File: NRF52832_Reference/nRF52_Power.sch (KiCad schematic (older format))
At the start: 21 parts

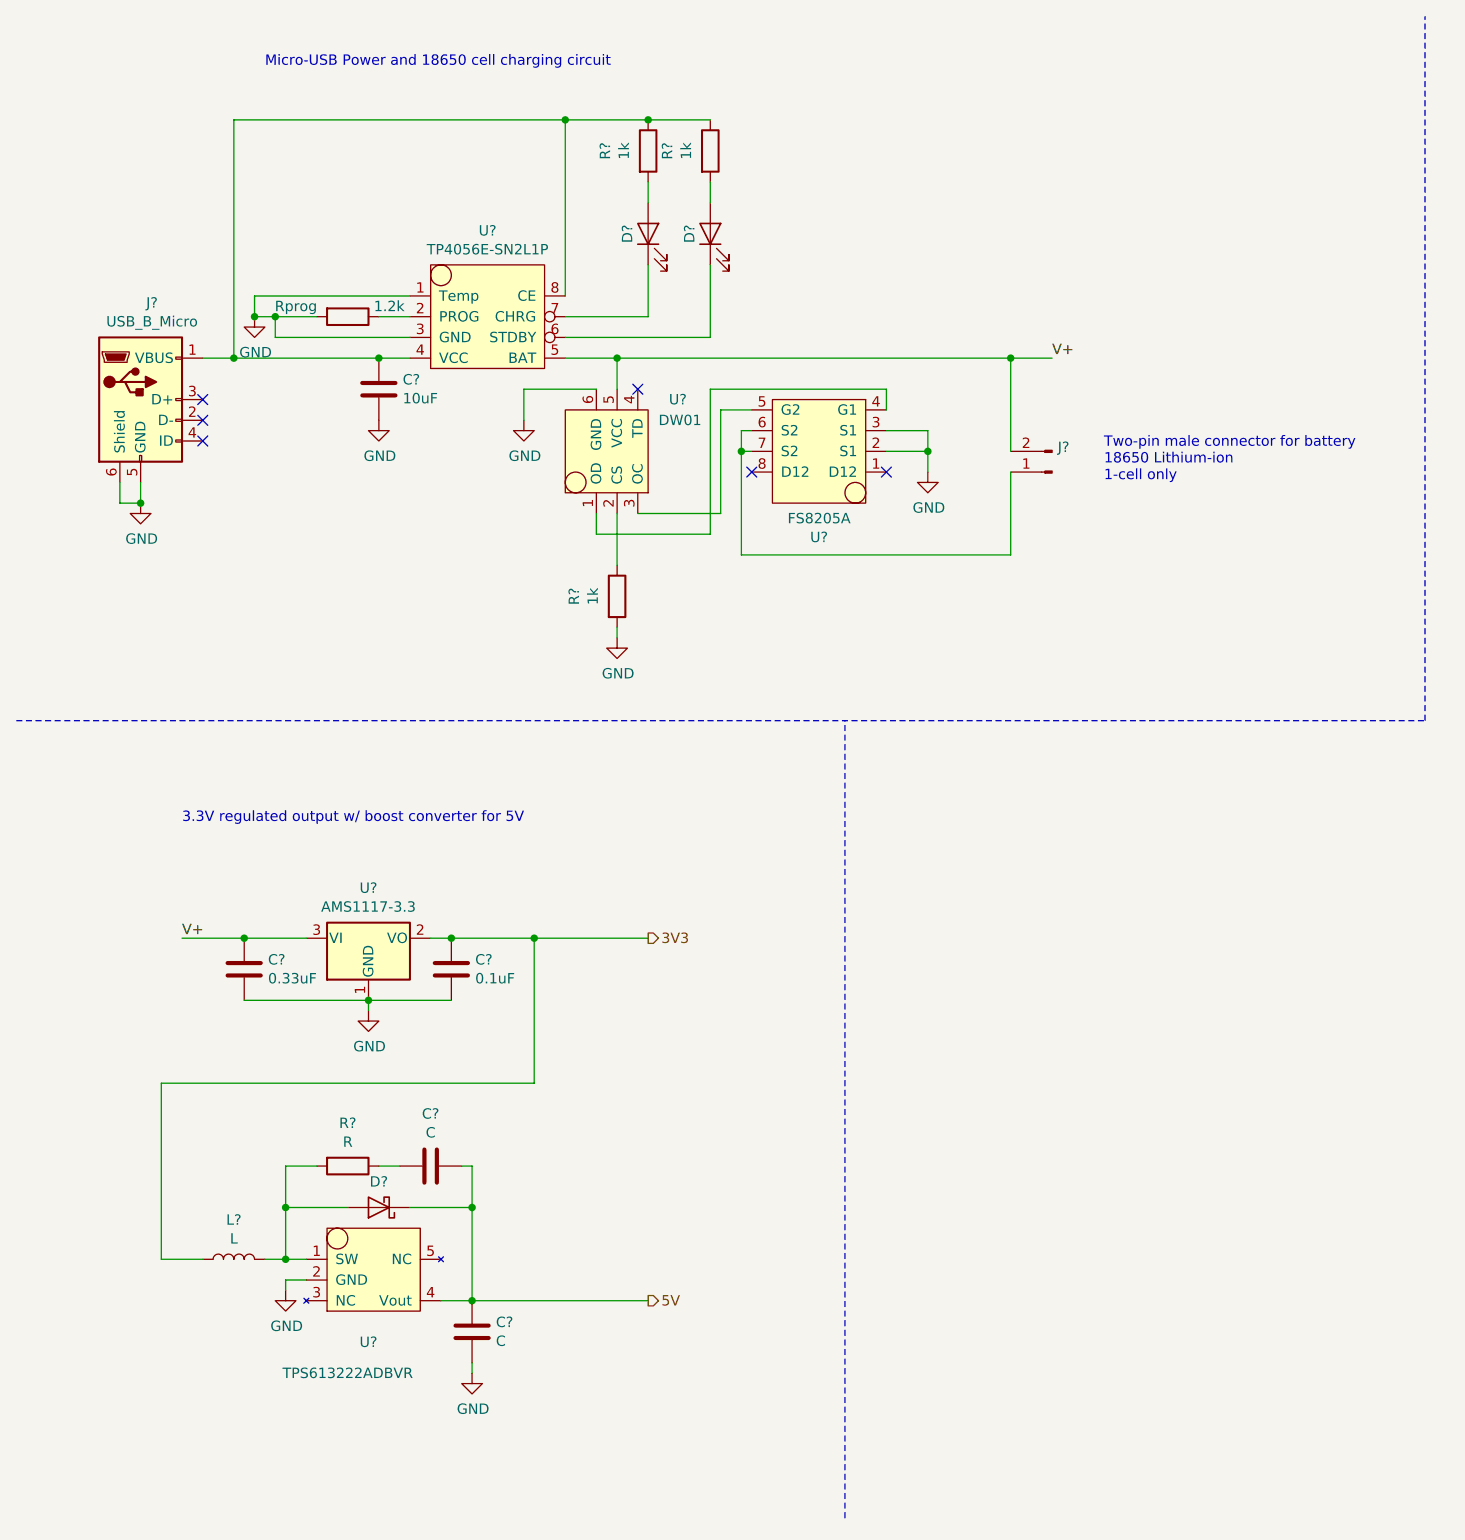
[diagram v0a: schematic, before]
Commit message: Added I2C components: 4KB EEPROM, Light sensor, and Temp sensor to schematic.
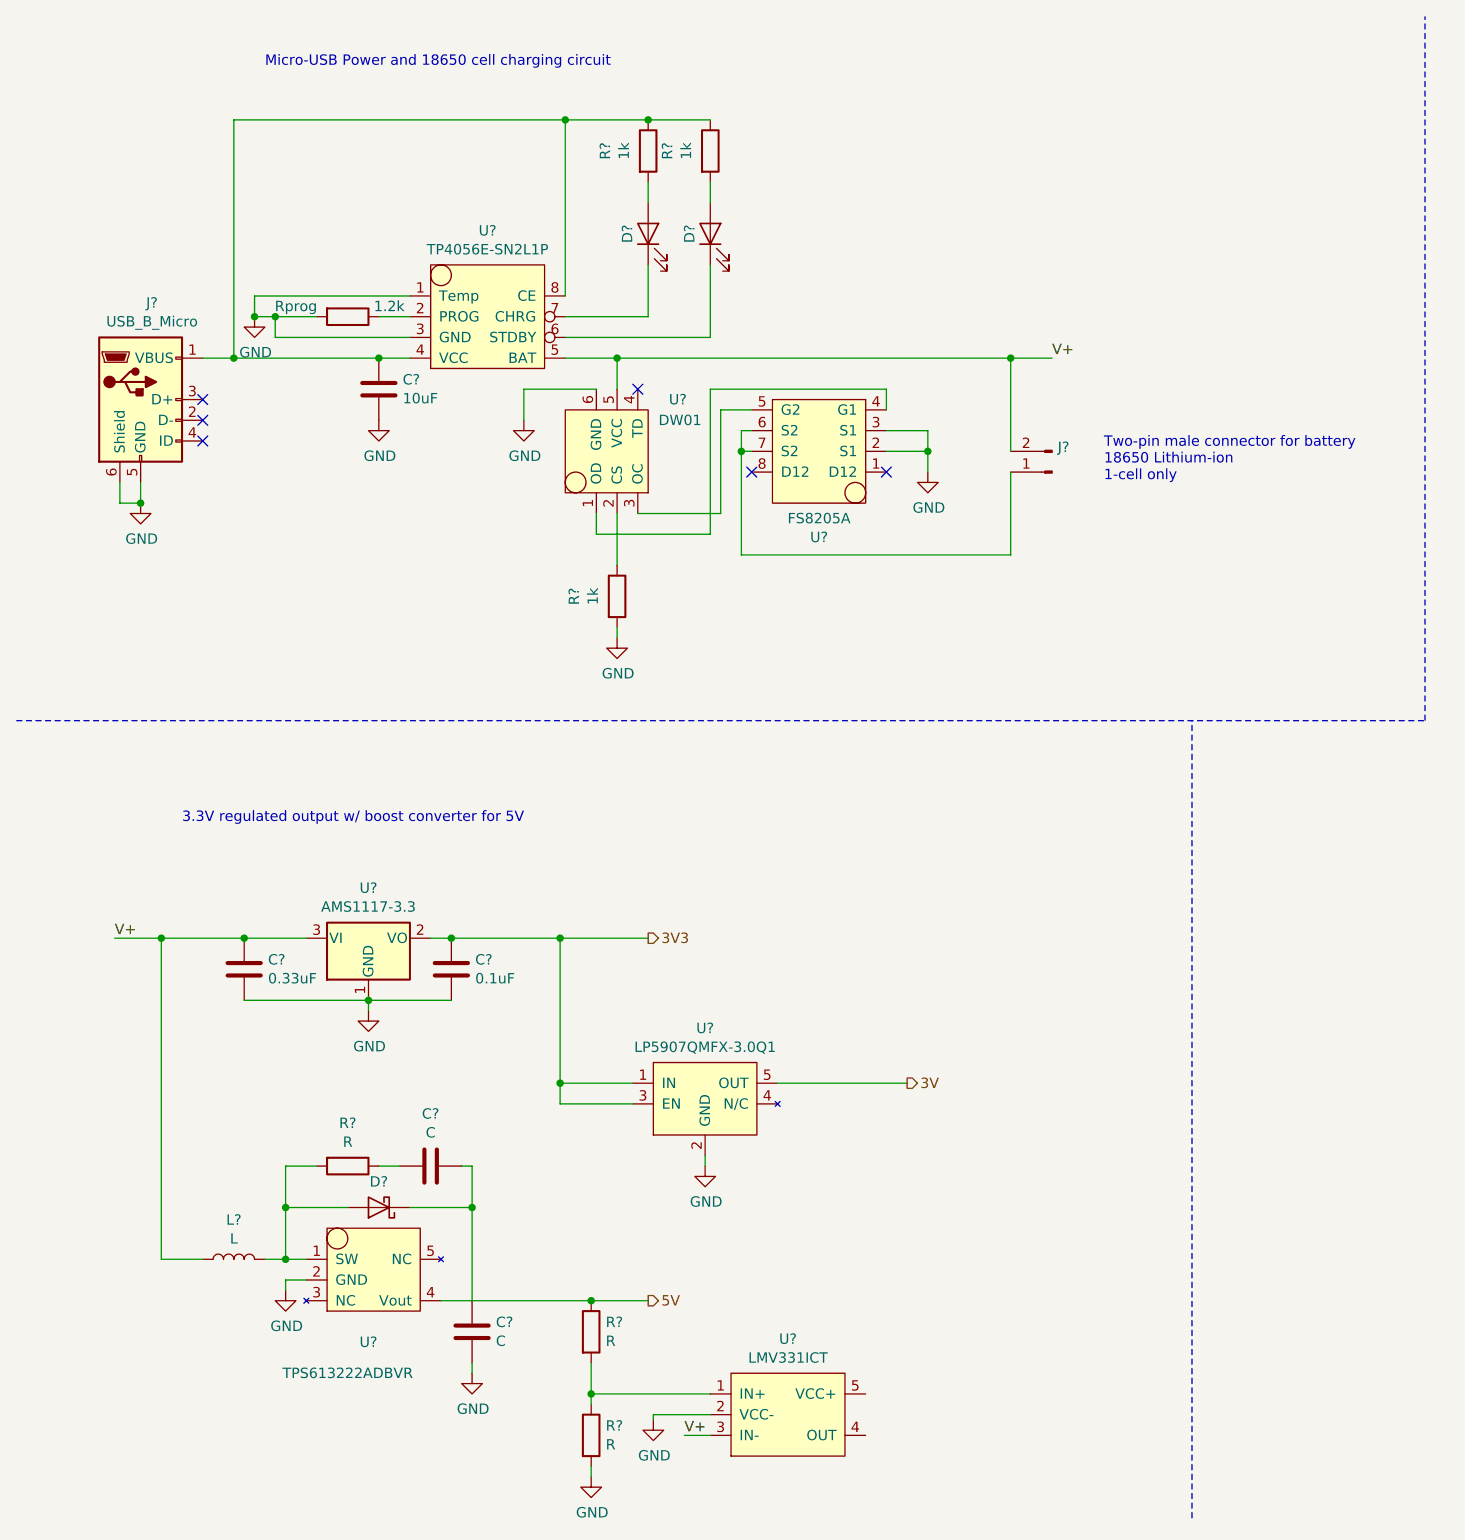
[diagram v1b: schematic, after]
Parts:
- added R? (x2): R, symbol Device:R
- added U?: LP5907QMFX-3.0Q1, symbol Project_Libary:LP5907QMFX-3.0Q1
- added U?: LMV331ICT, symbol Project_Libary:LMV331ICT
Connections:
- net 3V3: now also U?.1 (IN), U?.3 (EN); no longer L?.1
- net 5V: now also R?.1; no longer C?.1, C?.1, D?.1 (K)
- net GND: now also R?.2, U?.2 (GND), U?.2 (VCC-)
- net V+: now also L?.1, U?.3 (IN-)
- new net: C?.1, C?.1, D?.1 (K)
- new net: R?.1, R?.2, U?.1 (IN+)
- new net 3V: U?.5 (OUT)
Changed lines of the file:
@@
 Connection ~ 1600 4950
-Wire Wire Line
-	1600 4950 1300 4950
-Wire Wire Line
-	2600 4950 3000 4950
 Wire Wire Line
 	1600 5250 2200 5250
@@
 Wire Wire Line
 	1800 6600 1800 6650
-Wire Wire Line
-	3000 4950 3000 5650
-Connection ~ 3000 4950
-Wire Wire Line
-	3000 4950 3550 4950
 $Comp
 L Device:L L?
@@
 Wire Wire Line
 	1400 6500 1200 6500
-Text Label 1300 4950 0    50   ~ 0
+Text Label 975  4950 0    50   ~ 0
 V+
 Wire Wire Line
@@
 Wire Wire Line
 	2250 6050 2350 6050
-Connection ~ 2700 6700
-Wire Wire Line
-	2700 6700 2550 6700
-Wire Wire Line
-	3000 5650 1200 5650
-Wire Wire Line
-	1200 5650 1200 6500
 $Comp
 L power:GND #PWR?
@@
 Wire Wire Line
 	2700 7000 2700 7050
-Wire Wire Line
-	2700 6700 3550 6700
 Wire Wire Line
 	2700 6700 2700 6250
@@
 3.3V regulated output w/ boost converter for 5V
 Wire Notes Line
-	4500 7750 4500 3900
+	6175 7750 6175 3900
+Wire Wire Line
+	2600 4950 3125 4950
+Wire Wire Line
+	1200 4950 1600 4950
+Wire Wire Line
+	1200 4950 1200 6500
+Wire Wire Line
+	1200 4950 975  4950
+Connection ~ 1200 4950
+Wire Wire Line
+	2550 6700 3275 6700
+$Comp
+L Project_Libary:LP5907QMFX-3.0Q1 U?
+U 1 1 5C08E5C3
+P 3825 5700
+F 0 "U?" H 3825 6015 50  0000 C CNN
+F 1 "LP5907QMFX-3.0Q1" H 3825 5924 50  0000 C CNN
+F 2 "" H 3775 6150 50  0001 C CNN
+F 3 "" H 3775 6150 50  0001 C CNN
+	1    3825 5700
+	1    0    0    -1
+$EndComp
+Wire Wire Line
+	3475 5650 3125 5650
+Wire Wire Line
+	3125 5650 3125 4950
+Connection ~ 3125 4950
+Wire Wire Line
+	3125 4950 3550 4950
+Wire Wire Line
+	3475 5750 3125 5750
+Wire Wire Line
+	3125 5750 3125 5650
+Connection ~ 3125 5650
+$Comp
+L power:GND #PWR?
+U 1 1 5C096B77
+P 3825 6050
+AR Path="/5C096B77" Ref="#PWR?"  Part="1"
+AR Path="/5BF31556/5C096B77" Ref="#PWR?"  Part="1"
+F 0 "#PWR?" H 3825 5800 50  0001 C CNN
+F 1 "GND" H 3830 5877 50  0000 C CNN
+F 2 "" H 3825 6050 50  0001 C CNN
+F 3 "" H 3825 6050 50  0001 C CNN
+	1    3825 6050
+	1    0    0    -1
+$EndComp
+Wire Wire Line
+	3825 6000 3825 6050
+Wire Wire Line
+	4175 5650 4800 5650
+Text HLabel 4800 5650 2    50   Output ~ 0
+3V
+$Comp
+L Project_Libary:LMV331ICT U?
+U 1 1 5C09D77C
+P 4200 7250
+F 0 "U?" H 4225 7615 50  0000 C CNN
+F 1 "LMV331ICT" H 4225 7524 50  0000 C CNN
+F 2 "" H 4150 7550 50  0001 C CNN
+F 3 "" H 4150 7550 50  0001 C CNN
+	1    4200 7250
+	1    0    0    -1
+$EndComp
+$Comp
+L Device:R R?
+U 1 1 5C0A05AB
+P 3275 6850
+F 0 "R?" H 3345 6896 50  0000 L CNN
+F 1 "R" H 3345 6805 50  0000 L CNN
+F 2 "" V 3205 6850 50  0001 C CNN
+F 3 "~" H 3275 6850 50  0001 C CNN
+	1    3275 6850
+	1    0    0    -1
+$EndComp
+Connection ~ 3275 6700
+Wire Wire Line
+	3275 6700 3550 6700
+$Comp
+L Device:R R?
+U 1 1 5C0A072D
+P 3275 7350
+F 0 "R?" H 3345 7396 50  0000 L CNN
+F 1 "R" H 3345 7305 50  0000 L CNN
+F 2 "" V 3205 7350 50  0001 C CNN
+F 3 "~" H 3275 7350 50  0001 C CNN
+	1    3275 7350
+	1    0    0    -1
+$EndComp
+$Comp
+L power:GND #PWR?
+U 1 1 5C0A07A3
+P 3275 7550
+AR Path="/5C0A07A3" Ref="#PWR?"  Part="1"
+AR Path="/5BF31556/5C0A07A3" Ref="#PWR?"  Part="1"
+F 0 "#PWR?" H 3275 7300 50  0001 C CNN
+F 1 "GND" H 3280 7377 50  0000 C CNN
+F 2 "" H 3275 7550 50  0001 C CNN
+F 3 "" H 3275 7550 50  0001 C CNN
+	1    3275 7550
+	1    0    0    -1
+$EndComp
+Wire Wire Line
+	3275 7000 3275 7150
+Wire Wire Line
+	3275 7500 3275 7550
+Wire Wire Line
+	3850 7150 3275 7150
+Connection ~ 3275 7150
+Wire Wire Line
+	3275 7150 3275 7200
+$Comp
+L power:GND #PWR?
+U 1 1 5C0A675B
+P 3575 7275
+AR Path="/5C0A675B" Ref="#PWR?"  Part="1"
+AR Path="/5BF31556/5C0A675B" Ref="#PWR?"  Part="1"
+F 0 "#PWR?" H 3575 7025 50  0001 C CNN
+F 1 "GND" H 3580 7102 50  0000 C CNN
+F 2 "" H 3575 7275 50  0001 C CNN
+F 3 "" H 3575 7275 50  0001 C CNN
+	1    3575 7275
+	1    0    0    -1
+$EndComp
+Wire Wire Line
+	3850 7250 3575 7250
+Wire Wire Line
+	3575 7250 3575 7275
+Wire Wire Line
+	3850 7350 3725 7350
+Text Label 3725 7350 0    50   ~ 0
+V+
 $EndSCHEMATC

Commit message: Updated Boost conv. components and moved 3.3V regulator.
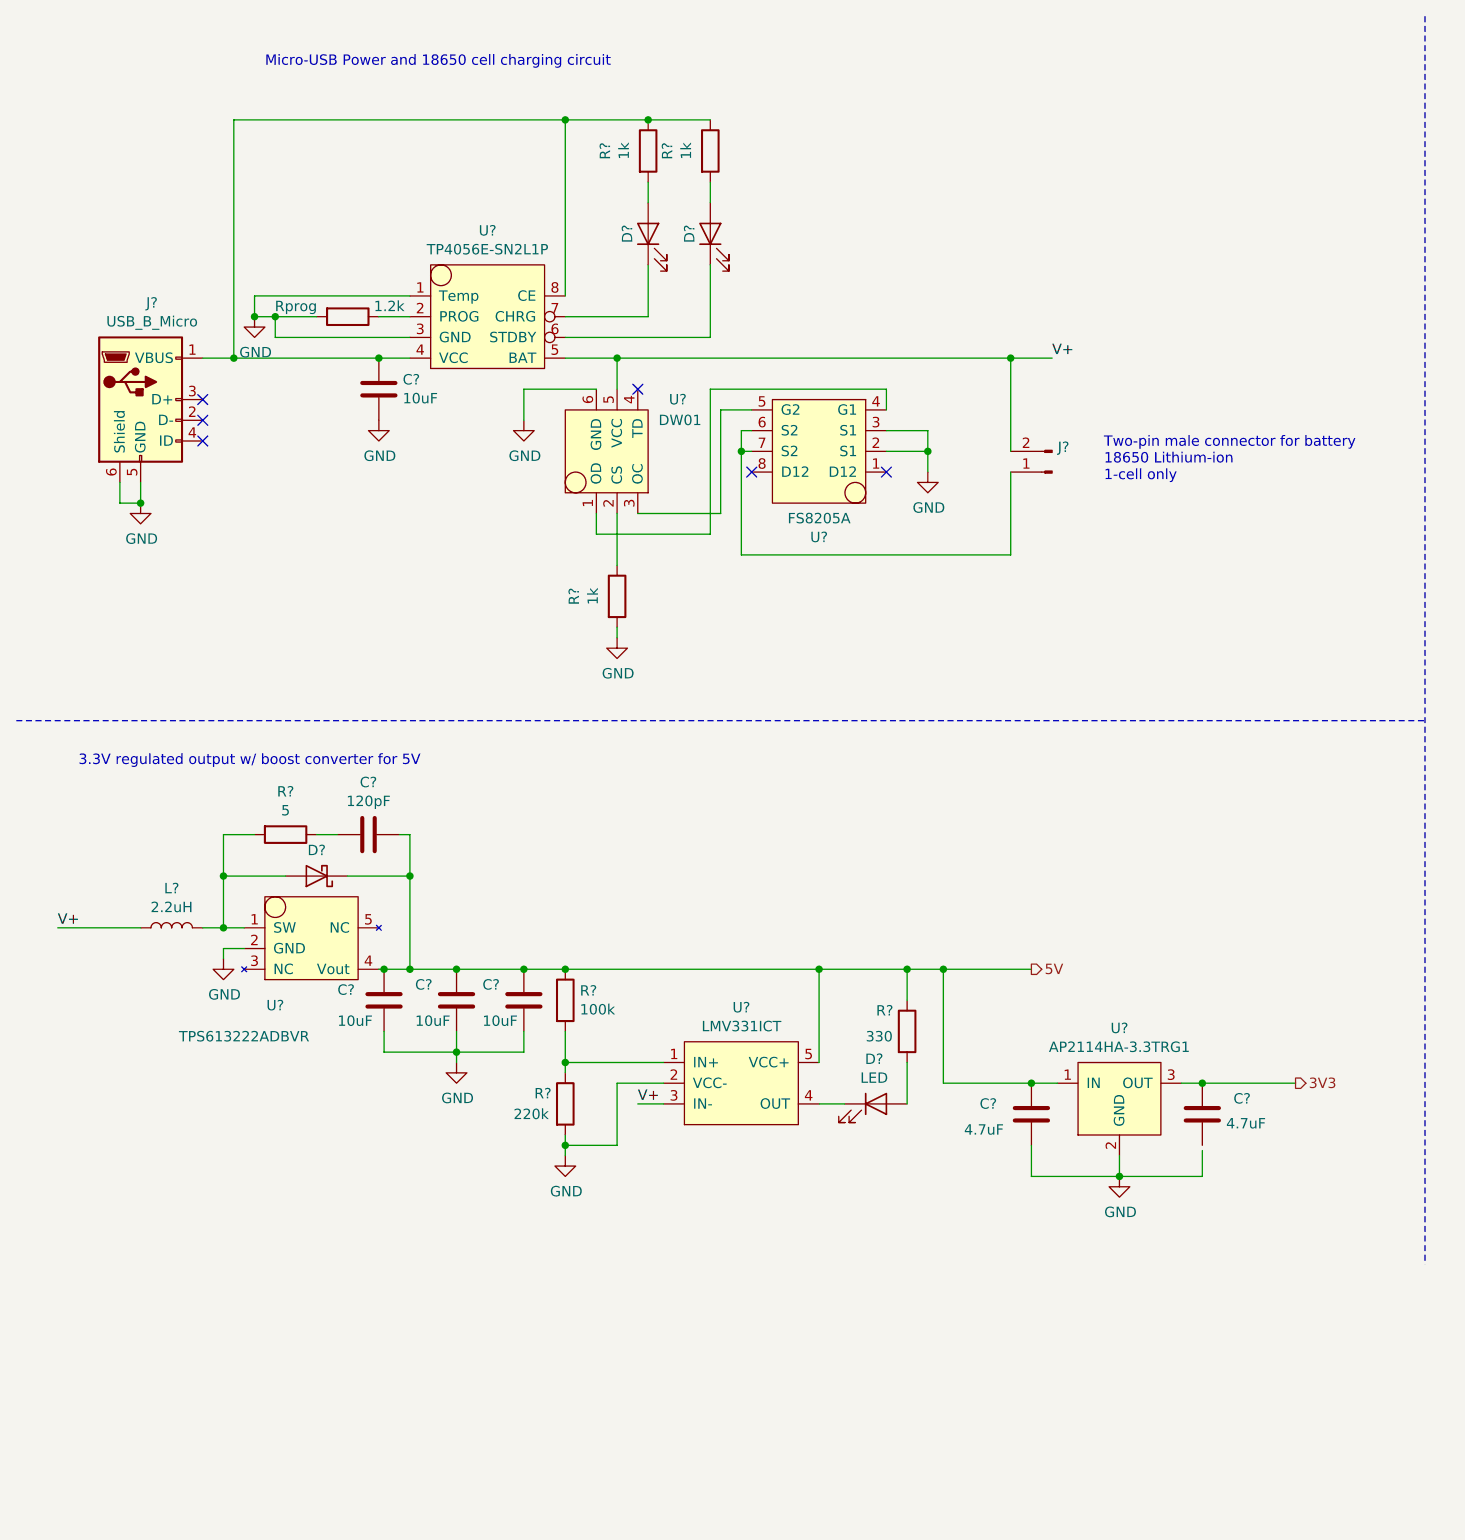
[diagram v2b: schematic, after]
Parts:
- removed U?: AMS1117-3.3, Package_TO_SOT_SMD:SOT-223-3_TabPin2, symbol Regulator_Linear:AMS1117-3.3
- removed U?: LP5907QMFX-3.0Q1, symbol Project_Libary:LP5907QMFX-3.0Q1
- added C? (x2): 10uF, symbol Device:C
- added D?: LED, symbol Device:LED
- added R?: 330, symbol Device:R
- added U?: AP2114HA-3.3TRG1, symbol Project_Libary:AP2114HA-3.3TRG1
- C?: value 0.33uF -> 4.7uF
- C?: value 0.1uF -> 4.7uF
- C?: value C -> 10uF
- C?: value C -> 120pF
- L?: value L -> 2.2uH
- R?: value R -> 5
- R?: value R -> 100k
- R?: value R -> 220k
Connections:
- net 3V3: now also U?.3 (OUT)
- net 5V: now also C?.1, C?.1, C?.1, D?.1 (K), U?.5 (VCC+), C?.1, C?.1, R?.1, U?.1 (IN)
- net GND: now also C?.2, C?.2, U?.2 (GND); no longer C?.2
- net V+: no longer C?.1
- net at U?.4 (OUT): now also D?.1 (K)
- new net: D?.2 (A), R?.2
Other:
- moved on the sheet: C?, D?, L?, R?, U?
